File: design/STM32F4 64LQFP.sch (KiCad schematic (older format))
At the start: 16 parts, among them P2 SWD, U1 STM32F40X_LQFP64, X2 8MHz 10ppm

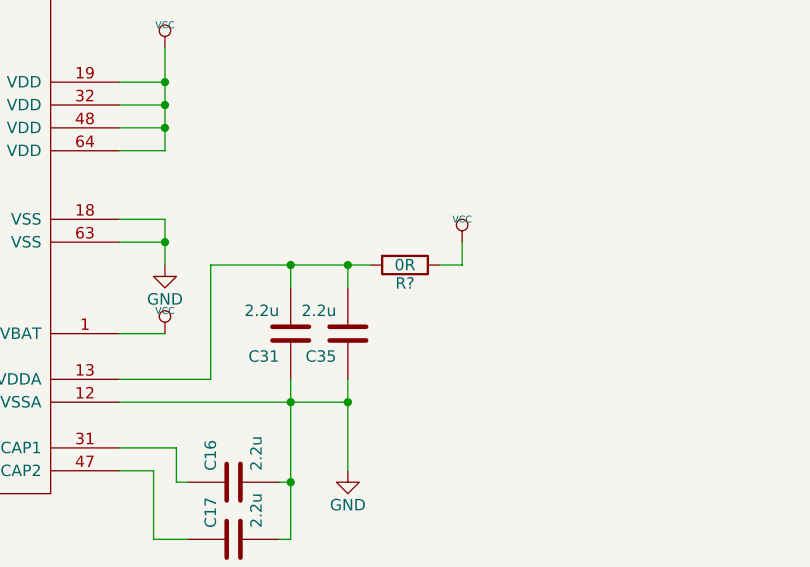
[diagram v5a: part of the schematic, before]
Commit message: Assigned some footprints.
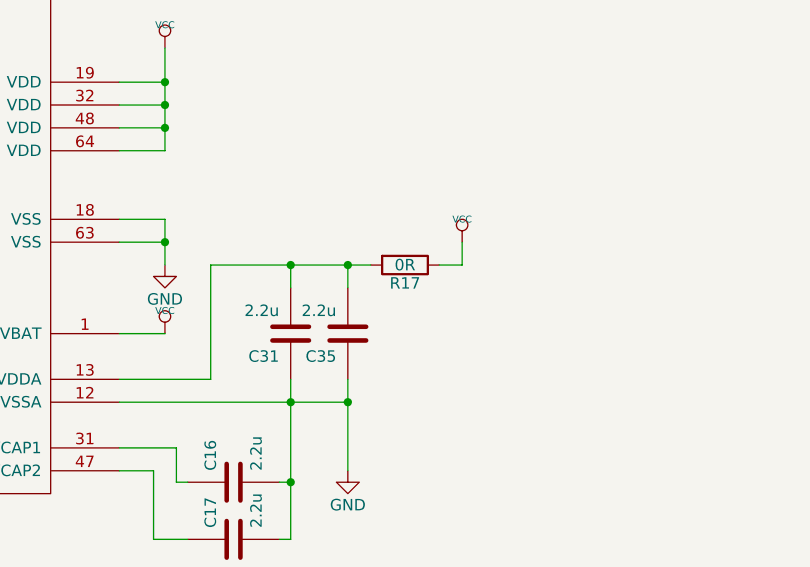
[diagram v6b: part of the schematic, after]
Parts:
- C10, C11, C12, C13, C14, C15, C16, C17, C31, C32, C35, C38: footprint SMD_Packages:SMD-0603_c -> Capacitors_SMD:C_0603
- gave numbers to parts that had none: 1
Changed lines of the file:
@@
 F 0 "C17" H 7550 6450 50  0000 L CNN
 F 1 "2.2u" H 7550 6250 50  0000 L CNN
-F 2 "SMD_Packages:SMD-0603_c" H 7500 6350 60  0001 C CNN
+F 2 "Capacitors_SMD:C_0603" H 7500 6350 60  0001 C CNN
 F 3 "" H 7500 6350 60  0001 C CNN
 	1    7500 6350
@@
 F 0 "C16" H 7550 6200 50  0000 L CNN
 F 1 "2.2u" H 7550 6000 50  0000 L CNN
-F 2 "SMD_Packages:SMD-0603_c" H 7500 6100 60  0001 C CNN
+F 2 "Capacitors_SMD:C_0603" H 7500 6100 60  0001 C CNN
 F 3 "" H 7500 6100 60  0001 C CNN
 	1    7500 6100
@@
 $EndComp
 $Comp
-L VCC #PWR036
+L VCC #PWR027
 U 1 1 53F757C2
 P 8500 5050
-F 0 "#PWR036" H 8500 5150 30  0001 C CNN
+F 0 "#PWR027" H 8500 5150 30  0001 C CNN
 F 1 "VCC" H 8500 5150 30  0000 C CNN
 F 2 "" H 8500 5050 60  0001 C CNN
@@
 $EndComp
 $Comp
-L VCC #PWR038
+L VCC #PWR028
 U 1 1 53F757CE
 P 7200 4200
-F 0 "#PWR038" H 7200 4300 30  0001 C CNN
+F 0 "#PWR028" H 7200 4300 30  0001 C CNN
 F 1 "VCC" H 7200 4300 30  0000 C CNN
 F 2 "" H 7200 4200 60  0001 C CNN
@@
 F 0 "C15" H 7400 1900 50  0000 L CNN
 F 1 "15p" H 7400 1700 50  0000 L CNN
-F 2 "SMD_Packages:SMD-0603_c" H 7350 1800 60  0001 C CNN
+F 2 "Capacitors_SMD:C_0603" H 7350 1800 60  0001 C CNN
 F 3 "" H 7350 1800 60  0001 C CNN
 	1    7350 1800
@@
 F 0 "C38" H 8150 1900 50  0000 L CNN
 F 1 "15p" H 8150 1700 50  0000 L CNN
-F 2 "SMD_Packages:SMD-0603_c" H 8100 1800 60  0001 C CNN
+F 2 "Capacitors_SMD:C_0603" H 8100 1800 60  0001 C CNN
 F 3 "" H 8100 1800 60  0001 C CNN
 	1    8100 1800
@@
 $EndComp
 $Comp
-L GND-RESCUE-BLDC_4 #PWR039
+L GND-RESCUE-BLDC_4 #PWR029
 U 1 1 53F757E9
 P 8250 1600
-F 0 "#PWR039" H 8250 1600 30  0001 C CNN
+F 0 "#PWR029" H 8250 1600 30  0001 C CNN
 F 1 "GND" H 8250 1530 30  0001 C CNN
 F 2 "" H 8250 1600 60  0001 C CNN
@@
 F 0 "C31" H 7800 5550 50  0000 L CNN
 F 1 "2.2u" H 7800 5350 50  0000 L CNN
-F 2 "SMD_Packages:SMD-0603_c" H 7750 5450 60  0001 C CNN
+F 2 "Capacitors_SMD:C_0603" H 7750 5450 60  0001 C CNN
 F 3 "" H 7750 5450 60  0001 C CNN
 	1    7750 5450
@@
 F 0 "C35" H 8050 5550 50  0000 L CNN
 F 1 "2.2u" H 8050 5350 50  0000 L CNN
-F 2 "SMD_Packages:SMD-0603_c" H 8000 5450 60  0001 C CNN
+F 2 "Capacitors_SMD:C_0603" H 8000 5450 60  0001 C CNN
 F 3 "" H 8000 5450 60  0001 C CNN
 	1    8000 5450
@@
 NoConn ~ 7000 2450
 $Comp
-L VCC #PWR041
+L VCC #PWR030
 U 1 1 53F75807
 P 7200 5450
-F 0 "#PWR041" H 7200 5550 30  0001 C CNN
+F 0 "#PWR030" H 7200 5550 30  0001 C CNN
 F 1 "VCC" H 7200 5550 30  0000 C CNN
 F 2 "" H 7200 5450 60  0001 C CNN
@@
 F 0 "C32" H 8000 3200 50  0000 L CNN
 F 1 "100n" H 8000 3000 50  0000 L CNN
-F 2 "SMD_Packages:SMD-0603_c" H 7950 3100 60  0001 C CNN
+F 2 "Capacitors_SMD:C_0603" H 7950 3100 60  0001 C CNN
 F 3 "" H 7950 3100 60  0001 C CNN
 	1    7950 3100
@@
 $EndComp
 $Comp
-L VCC #PWR043
+L VCC #PWR031
 U 1 1 53F77417
 P 9900 2750
-F 0 "#PWR043" H 9900 2850 30  0001 C CNN
+F 0 "#PWR031" H 9900 2850 30  0001 C CNN
 F 1 "VCC" H 9900 2850 30  0000 C CNN
 F 2 "" H 9900 2750 60  0001 C CNN
@@
 F 0 "C10" H 9450 1400 50  0000 L CNN
 F 1 "2.2u" H 9450 1200 50  0000 L CNN
-F 2 "SMD_Packages:SMD-0603_c" H 9400 1300 60  0001 C CNN
+F 2 "Capacitors_SMD:C_0603" H 9400 1300 60  0001 C CNN
 F 3 "" H 9400 1300 60  0001 C CNN
 	1    9400 1300
@@
 F 0 "C11" H 9700 1400 50  0000 L CNN
 F 1 "2.2u" H 9700 1200 50  0000 L CNN
-F 2 "SMD_Packages:SMD-0603_c" H 9650 1300 60  0001 C CNN
+F 2 "Capacitors_SMD:C_0603" H 9650 1300 60  0001 C CNN
 F 3 "" H 9650 1300 60  0001 C CNN
 	1    9650 1300
@@
 F 0 "C14" H 10450 1400 50  0000 L CNN
 F 1 "2.2u" H 10450 1200 50  0000 L CNN
-F 2 "SMD_Packages:SMD-0603_c" H 10400 1300 60  0001 C CNN
+F 2 "Capacitors_SMD:C_0603" H 10400 1300 60  0001 C CNN
 F 3 "" H 10400 1300 60  0001 C CNN
 	1    10400 1300
@@
 $EndComp
 $Comp
-L GND-RESCUE-BLDC_4 #PWR045
+L GND-RESCUE-BLDC_4 #PWR032
 U 1 1 53F7743B
 P 9100 1650
-F 0 "#PWR045" H 9100 1650 30  0001 C CNN
+F 0 "#PWR032" H 9100 1650 30  0001 C CNN
 F 1 "GND" H 9100 1580 30  0001 C CNN
 F 2 "" H 9100 1650 60  0001 C CNN
@@
 $EndComp
 $Comp
-L VCC #PWR046
+L VCC #PWR033
 U 1 1 53F77441
 P 9100 950
-F 0 "#PWR046" H 9100 1050 30  0001 C CNN
+F 0 "#PWR033" H 9100 1050 30  0001 C CNN
 F 1 "VCC" H 9100 1050 30  0000 C CNN
 F 2 "" H 9100 950 60  0001 C CNN
@@
 F 0 "C12" H 9950 1400 50  0000 L CNN
 F 1 "2.2u" H 9950 1200 50  0000 L CNN
-F 2 "SMD_Packages:SMD-0603_c" H 9900 1300 60  0001 C CNN
+F 2 "Capacitors_SMD:C_0603" H 9900 1300 60  0001 C CNN
 F 3 "" H 9900 1300 60  0001 C CNN
 	1    9900 1300
@@
 F 0 "C13" H 10200 1400 50  0000 L CNN
 F 1 "2.2u" H 10200 1200 50  0000 L CNN
-F 2 "SMD_Packages:SMD-0603_c" H 10150 1300 60  0001 C CNN
+F 2 "Capacitors_SMD:C_0603" H 10150 1300 60  0001 C CNN
 F 3 "" H 10150 1300 60  0001 C CNN
 	1    10150 1300
@@
 $EndComp
 $Comp
-L GND-RESCUE-BLDC_4 #PWR047
+L GND-RESCUE-BLDC_4 #PWR034
 U 1 1 54097D19
 P 7750 2150
-F 0 "#PWR047" H 7750 2150 30  0001 C CNN
+F 0 "#PWR034" H 7750 2150 30  0001 C CNN
 F 1 "GND" H 7750 2080 30  0001 C CNN
 F 2 "" H 7750 2150 60  0001 C CNN
@@
 USART1_RX
 $Comp
-L GND #PWR?
+L GND #PWR035
 U 1 1 55E72202
 P 7150 2550
-F 0 "#PWR?" H 7150 2300 50  0001 C CNN
+F 0 "#PWR035" H 7150 2300 50  0001 C CNN
 F 1 "GND" H 7150 2400 50  0000 C CNN
 F 2 "" H 7150 2550 60  0000 C CNN
@@
 $EndComp
 $Comp
-L GND #PWR?
+L GND #PWR036
 U 1 1 55E72244
 P 7950 3300
-F 0 "#PWR?" H 7950 3050 50  0001 C CNN
+F 0 "#PWR036" H 7950 3050 50  0001 C CNN
 F 1 "GND" H 7950 3150 50  0000 C CNN
 F 2 "" H 7950 3300 60  0000 C CNN
@@
 $EndComp
 $Comp
-L GND #PWR?
+L GND #PWR037
 U 1 1 55E72286
 P 9600 3100
-F 0 "#PWR?" H 9600 2850 50  0001 C CNN
+F 0 "#PWR037" H 9600 2850 50  0001 C CNN
 F 1 "GND" H 9600 2950 50  0000 C CNN
 F 2 "" H 9600 3100 60  0000 C CNN
@@
 $EndComp
 $Comp
-L GND #PWR?
+L GND #PWR038
 U 1 1 55E72368
 P 7200 5150
-F 0 "#PWR?" H 7200 4900 50  0001 C CNN
+F 0 "#PWR038" H 7200 4900 50  0001 C CNN
 F 1 "GND" H 7200 5000 50  0000 C CNN
 F 2 "" H 7200 5150 60  0000 C CNN
@@
 $EndComp
 $Comp
-L GND #PWR?
+L GND #PWR039
 U 1 1 55E723AA
 P 8000 6050
-F 0 "#PWR?" H 8000 5800 50  0001 C CNN
+F 0 "#PWR039" H 8000 5800 50  0001 C CNN
 F 1 "GND" H 8000 5900 50  0000 C CNN
 F 2 "" H 8000 6050 60  0000 C CNN
@@
 	7400 5150 7400 5650
 $Comp
-L R R?
+L R R17
 U 1 1 55E738BB
 P 8250 5150
-F 0 "R?" V 8330 5150 50  0000 C CNN
+F 0 "R17" V 8330 5150 50  0000 C CNN
 F 1 "0R" V 8250 5150 50  0000 C CNN
-F 2 "" V 8180 5150 30  0000 C CNN
+F 2 "" V 8180 5150 30  0001 C CNN
 F 3 "" H 8250 5150 30  0000 C CNN
 	1    8250 5150

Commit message: Selected footprints
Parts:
- R17: footprint (none) -> Resistors_SMD:R_0603_HandSoldering
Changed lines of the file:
@@
 F 0 "R17" V 8330 5150 50  0000 C CNN
 F 1 "0R" V 8250 5150 50  0000 C CNN
-F 2 "" V 8180 5150 30  0001 C CNN
+F 2 "Resistors_SMD:R_0603_HandSoldering" V 8180 5150 30  0001 C CNN
 F 3 "" H 8250 5150 30  0000 C CNN
 	1    8250 5150

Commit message: Agreed programming connector with esden.
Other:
- note added: "Lisa/S Connector\nPin1: TMS/SWDIO\nPin2: GND\nPin3: TCK/SWCLK\nPin4: TDO/TRACESWO\nPin5: NRST\nStecker\n5-Pin 0.05" Pitch Pin Header"
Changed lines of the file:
@@
 Wire Wire Line
 	8500 5150 8400 5150
+Text Notes 10500 3450 0    60   ~ 0
+Lisa/S Connector\nPin1: TMS/SWDIO\nPin2: GND\nPin3: TCK/SWCLK\nPin4: TDO/TRACESWO\nPin5: NRST\nStecker\n5-Pin 0.05" Pitch Pin Header
 $EndSCHEMATC
